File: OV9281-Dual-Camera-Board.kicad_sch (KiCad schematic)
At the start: 83 parts, among them IC1 TLV73328PDBVT, IC2 TLV73318PDBVT, IC3 TLV73312PDBVT, J3 WE_68715014522, Q1 BSS138AKA, U1 OV9281, U2 OV9281, U3 NTS0104BQ, U4 NTB0104BQ, Y1 7C-24.000MBB-T, Y2 7C-24.000MBB-T

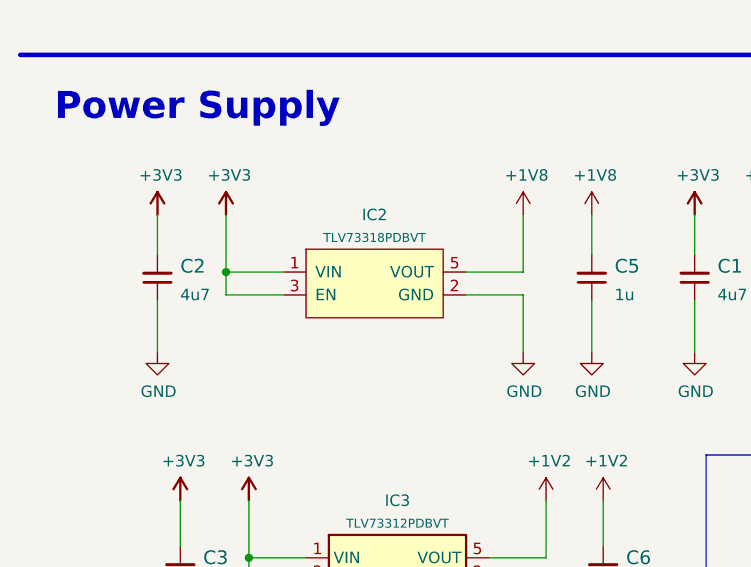
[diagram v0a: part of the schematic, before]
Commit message: Update TLV3318 to standardized version
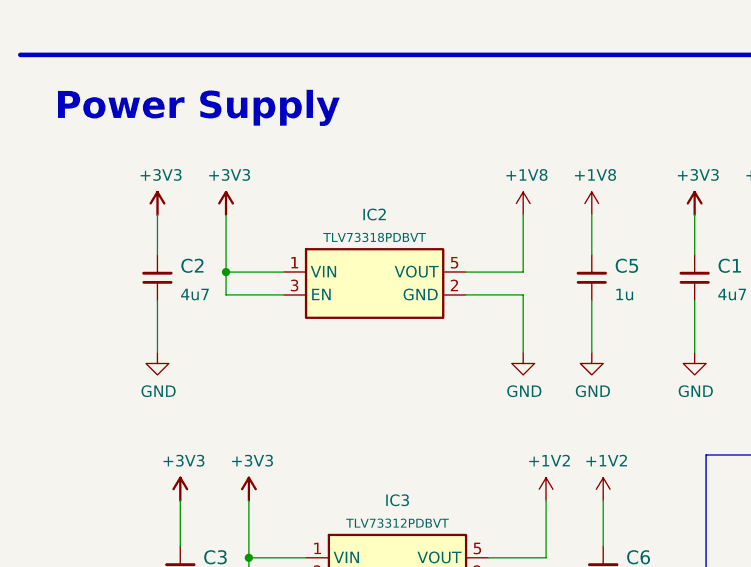
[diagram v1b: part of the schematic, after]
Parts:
- IC2: Author (none) -> Antmicro; License (none) -> Apache-2.0
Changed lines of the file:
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@@
     (stroke (width 0) (type default) (color 0 0 0 0))
   )
+  (wire (pts (xy 35.56 157.48) (xy 41.91 157.48))
+    (stroke (width 0) (type default) (color 0 0 0 0))
+  )
   (wire (pts (xy 134.62 93.98) (xy 134.62 97.79))
     (stroke (width 0) (type default) (color 0 0 0 0))
@@
     (stroke (width 0) (type default) (color 0 0 0 0))
   )
+  (wire (pts (xy 35.56 160.02) (xy 41.91 160.02))
+    (stroke (width 0) (type default) (color 0 0 0 0))
+  )
   (wire (pts (xy 195.58 207.01) (xy 205.74 207.01))
     (stroke (width 0) (type default) (color 0 0 0 0))
@@
     (stroke (width 0) (type default) (color 0 0 0 0))
   )
-  (wire (pts (xy 41.91 160.02) (xy 35.56 160.02))
-    (stroke (width 0) (type default) (color 0 0 0 0))
-  )
   (wire (pts (xy 55.88 119.38) (xy 54.61 119.38))
     (stroke (width 0) (type default) (color 0 0 0 0))
@@
     (stroke (width 0) (type default) (color 0 0 0 0))
   )
-  (wire (pts (xy 41.91 157.48) (xy 35.56 157.48))
-    (stroke (width 0) (type default) (color 0 0 0 0))
-  )
   (wire (pts (xy 165.1 115.57) (xy 163.83 115.57))
     (stroke (width 0) (type default) (color 0 0 0 0))
@@
     (pin "5")
   )
-  (symbol (lib_id "antmicroPMICVoltageRegulatorsLinear:TLV73318PDBVT") (at 52.07 158.75 0) (unit 1)
+  (symbol (lib_id "antmicroPMICVoltageRegulatorsLinear:TLV73318PDBVT") (at 41.91 157.48 0) (unit 1)
     (in_bom yes) (on_board yes) (fields_autoplaced)
     (property "Reference" "IC2" (id 0) (at 52.07 151.13 0))
@@
       (effects (font (size 0.9906 0.9906)))
     )
-    (property "Footprint" "antmicro-footprints:SOT-23-5" (id 2) (at 52.07 165.1 0)
+    (property "Footprint" "antmicro-footprints:SOT-23-5" (id 2) (at 41.91 163.83 0)
       (effects (font (size 1.27 1.27)) hide)
     )
-    (property "Datasheet" "" (id 3) (at 52.07 158.75 0)
+    (property "Datasheet" "https://www.ti.com/lit/ds/symlink/tlv733p.pdf?HQS=dis-dk-null-digikeymode-dsf-pf-null-wwe&ts=1694710748852&ref_url=https%253A%252F%252Fwww.ti.com%252Fgeneral%252Fdocs%252Fsuppproductinfo.tsp%253FdistId%253D10%2526gotoUrl%253Dhttps%253A%252F%252Fwww.ti.com%252Flit%252Fgpn%252Ftlv733p" (id 3) (at 41.91 157.48 0)
       (effects (font (size 1.27 1.27)) hide)
     )
-    (property "MPN" "TLV73318PDBVT" (id 4) (at 52.07 166.37 0)
+    (property "MPN" "TLV73318PDBVT" (id 4) (at 41.91 165.1 0)
       (effects (font (size 1.27 1.27)) hide)
     )
-    (property "Manufacturer" "Texas Instruments" (id 5) (at 52.07 168.91 0)
+    (property "Manufacturer" "Texas Instruments" (id 5) (at 41.91 167.64 0)
       (effects (font (size 1.27 1.27)) hide)
     )
+    (property "Author" "Antmicro" (id 6) (at 77.47 176.53 0)
+      (effects (font (size 1.27 1.27) (thickness 0.15)) (justify left bottom) hide)
+    )
+    (property "License" "Apache-2.0" (id 7) (at 77.47 179.07 0)
+      (effects (font (size 1.27 1.27) (thickness 0.15)) (justify left bottom) hide)
+    )
     (pin "1")

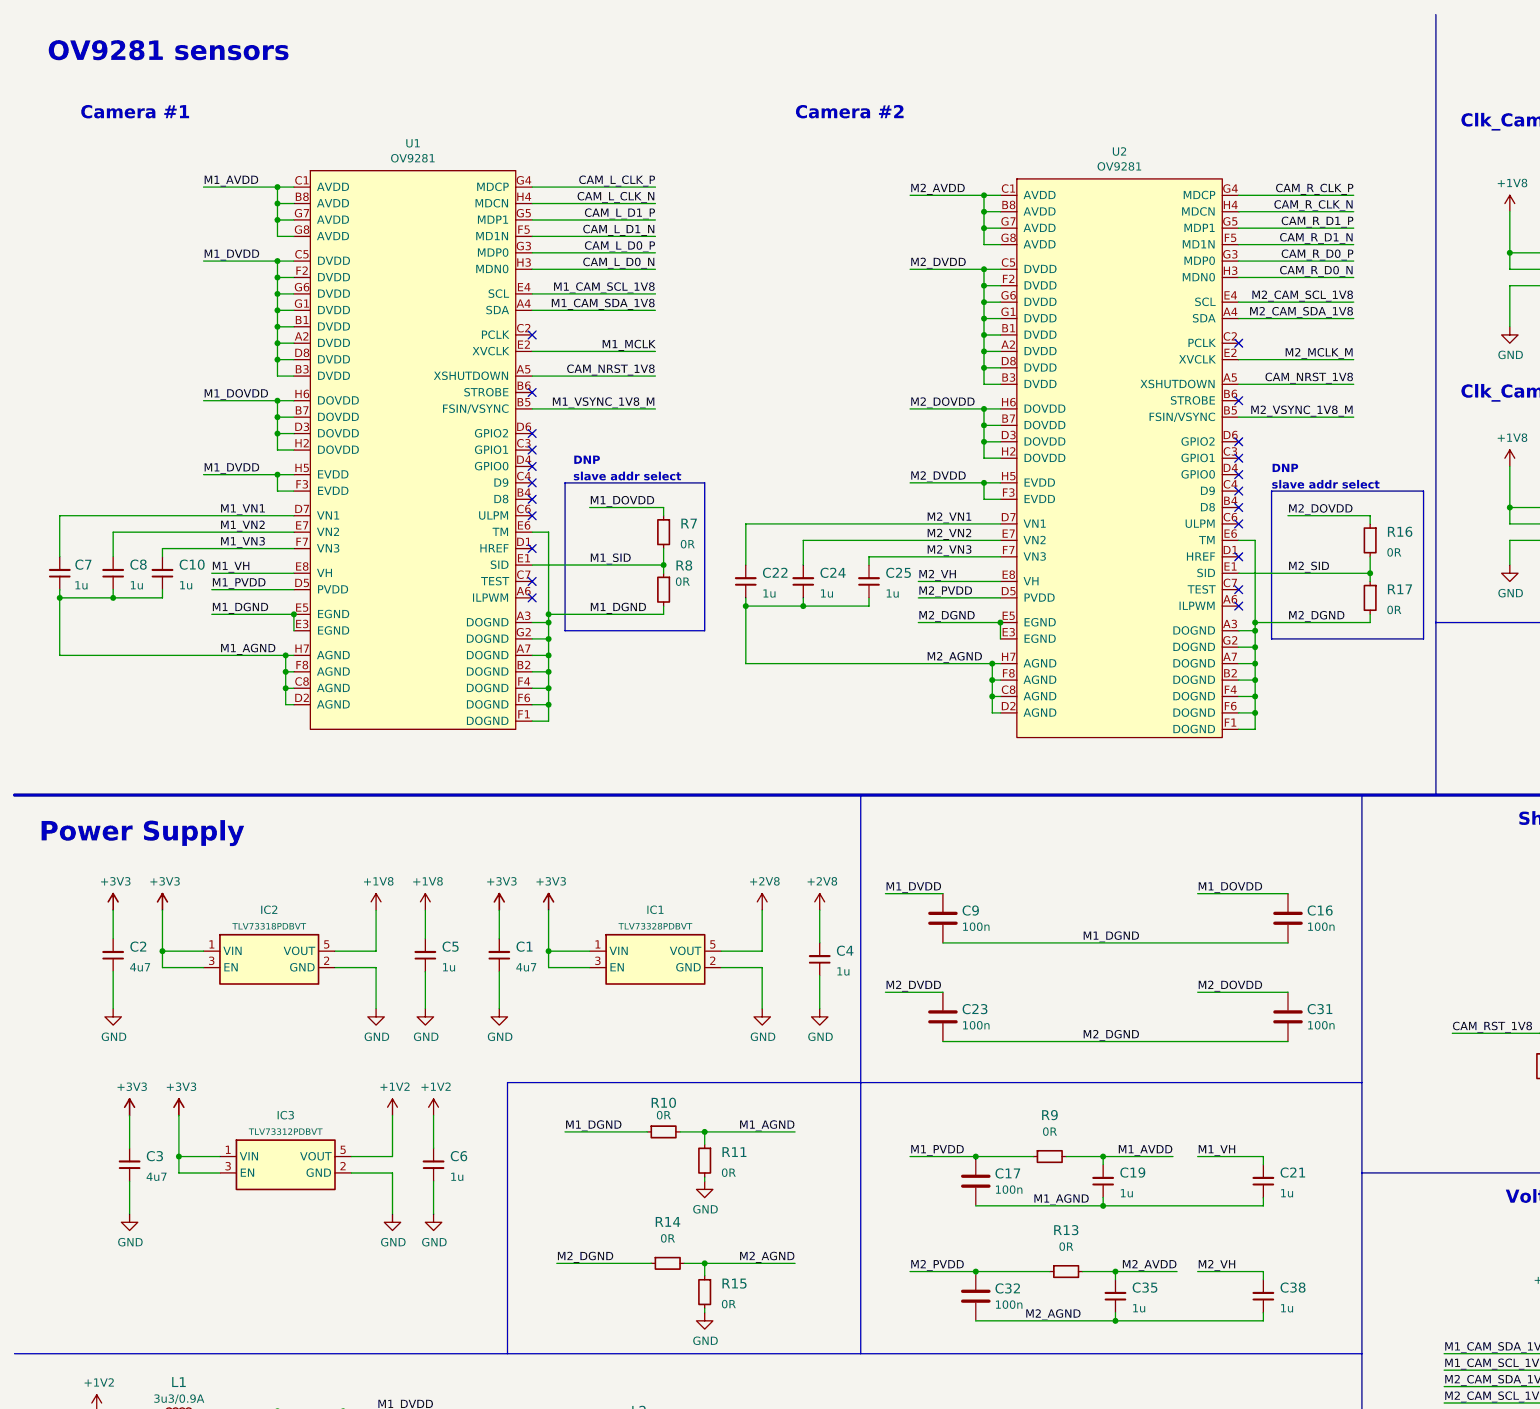
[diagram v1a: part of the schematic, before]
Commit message: Update OV9281
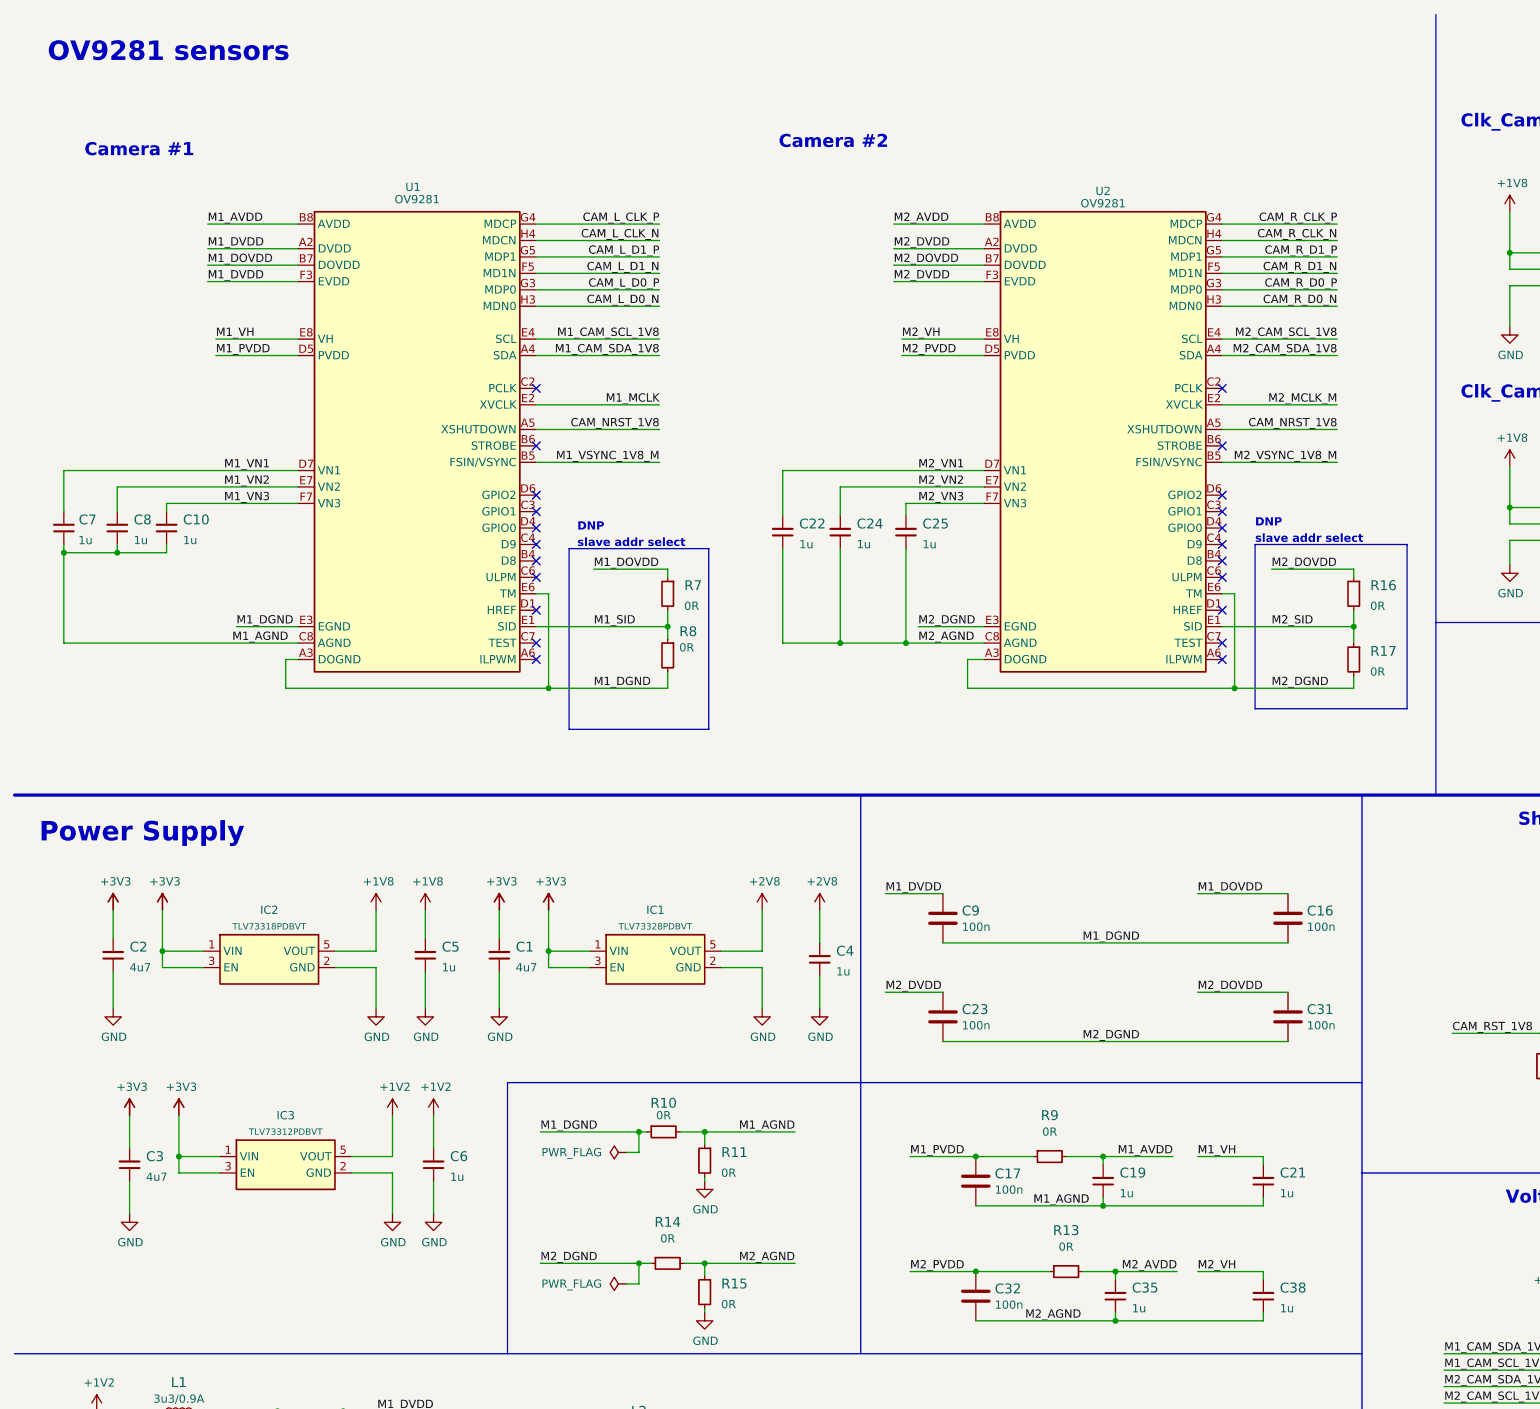
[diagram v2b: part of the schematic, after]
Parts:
- N1: footprint antmicro-footprints:antmicro-logo -> antmicro-footprints:antmicro-logo_scaled_12mm
- U1, U2: footprint antmicro-footprints:OV9281_camera_module -> antmicro-footprints:ImageSensor_OV9281; symbol antmicroCameramodules:OV9281 -> antmicroCameramodules:ImageSensor_OV9281; Author (none) -> Antmicro; License (none) -> Apache-2.0; Manufacturer OmniVision -> ARDUCAM
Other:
- moved on the sheet: C10, C22, C24, C25, C7, C8, R16, R17, R7, R8

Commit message: [#49221] Standardize schematic's symbols
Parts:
- C14, C15, C16, C17, C20, C23, C29, C30, C31, C32, C37, C9: value C_100n_0402_6V3 -> C_100n_6V3_0402; footprint OV9281-Dual-Camera-Board-footprints:0402-cap -> antmicro-footprints:C_0402_1005Metric; symbol OV9281-Dual-Camera-Board:C_100n_0402_6V3 -> antmicroCapacitorsmisc:C_100n_6V3_0402; Author (none) -> Antmicro; License (none) -> Apache-2.0
- J3: value WE_68715014522 -> Conn_FFC_WE_68715014522_TWO-SIDES; footprint OV9281-Dual-Camera-Board-footprints:WE_68715014522 -> antmicro-footprints:Conn_FFC_WE_68715014x22_ALT; symbol OV9281-Dual-Camera-Board:WE_68715014522 -> antmicroFCCConnectors:Conn_FFC_WE_68715014522_TWO-SIDES; Author (none) -> Antmicro; License (none) -> Apache-2.0; MPN 68715014522 -> 68715014522; Manufacturer Wurth ELEKTRONIK -> Würth Elektronik
- MP1, MP2, MP3, MP4: value PCB_Spacer_M2 -> Spacer_H3mm_9774030243R; footprint OV9281-Dual-Camera-Board-footprints:9774030243R -> antmicro-footprints:Spacer_SMD_M2_H3mm_Wurth_9774030243R; symbol OV9281-Dual-Camera-Board:PCB_Spacer_M2 -> antmicroMechanicalParts:Spacer_H3mm_9774030243R; Author (none) -> Antmicro; License (none) -> Apache-2.0; Manufacturer Wurth Elektronik -> Würth Elektronik
- MP5, MP6: value Camera_Lens -> Camera_Lens_20mm
- N1: footprint antmicro-footprints:antmicro-logo_scaled_12mm -> antmicro-footprints:antmicro-logo_scaled_20mm; Populate DNP -> (none); now left out of the parts list
- N2: now left out of the parts list
- Q1: value BSS138AKA -> BSS138PW; footprint antmicro-footprints:SOT-23-3 -> antmicro-footprints:SC70-3; symbol antmicroTransistorsFETsMOSFETsSingle:BSS138AKA -> antmicroTransistorsFETsMOSFETsSingle:BSS138PW; Author (none) -> Antmicro; License (none) -> Apache-2.0; MPN BSS138AKAR -> BSS138PW; Manufacturer ON Semiconductor -> Nexperia
- R1, R12, R2, R20, R22, R3, R4, R5, R6: Populate DNP -> (none)
- U1, U2: value OV9281 -> ImageSensor_OV9281
- renumbered IC2 to U5, IC3 to U6, IC1 to U7
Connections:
- net +1V2: now also C6.1; no longer C6.2
- net +1V8: now also C33.1, C34.1, C5.1; no longer C33.2, C34.2, C5.2
- net +2V8: now also C4.1; no longer C4.2
- net +3V3: now also C1.1, C2.1, C3.1; no longer C1.2, C2.2, C3.2
- net GND: now also C1.2, C2.2, C3.2, C33.2, C34.2, C4.2, C5.2, C6.2; no longer C1.1, C2.1, C3.1, C33.1, C34.1, C4.1, C5.1, C6.1
- net M1_AGND: now also C10.2, C18.2, C19.2, C21.2, C7.2, C8.2; no longer C10.1, C18.1, C19.1, C21.1, C7.1, C8.1
- net M1_AVDD: now also C18.1, C19.1; no longer C18.2, C19.2
- net M1_DGND: now also C12.2, C13.2; no longer C12.1, C13.1
- net M1_DOVDD: now also C13.1; no longer C13.2
- net M1_DVDD: now also C12.1; no longer C12.2
- net M1_VH: now also C21.1; no longer C21.2
- net M1_VN1: now also C7.1; no longer C7.2
- net M1_VN2: now also C8.1; no longer C8.2
- net M1_VN3: now also C10.1; no longer C10.2
- net M2_AGND: now also C22.2, C24.2, C25.2, C35.2, C36.2, C38.2; no longer C22.1, C24.1, C25.1, C35.1, C36.1, C38.1
- net M2_AVDD: now also C35.1, C36.1; no longer C35.2, C36.2
- net M2_DGND: now also C27.2, C28.2; no longer C27.1, C28.1
- net M2_DOVDD: now also C28.1; no longer C28.2
- net M2_DVDD: now also C27.1; no longer C27.2
- net M2_VH: now also C38.1; no longer C38.2
- net M2_VN1: now also C22.1; no longer C22.2
- net M2_VN2: now also C24.1; no longer C24.2
- net M2_VN3: now also C25.1; no longer C25.2
- no-connect marks 47 -> 49
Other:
- moved on the sheet: C1, C10, C12, C13, C14, C15, C16, C17, C18, C19, C2, C20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
